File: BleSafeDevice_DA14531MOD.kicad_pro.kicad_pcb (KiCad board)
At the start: 2 copper layers, 43.5 x 33.5 mm, 17 parts, among them J1 SWD_DEBUG_PADS, J2 CURRENT_MEAS_PADS, SW1 PTS526SK15SMTR2 LFS, U4 DA14531MOD-00F01002

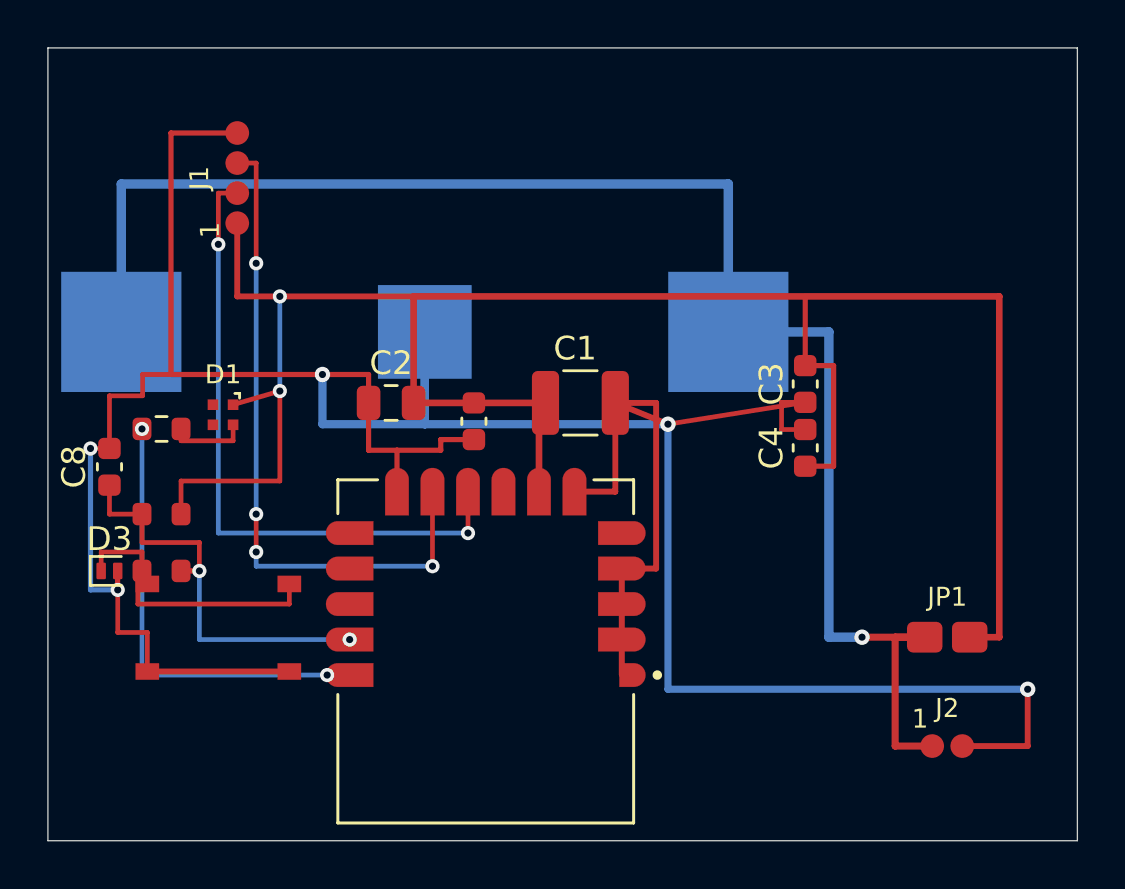
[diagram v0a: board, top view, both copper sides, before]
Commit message: Clear courtyard overlaps for prototype layout
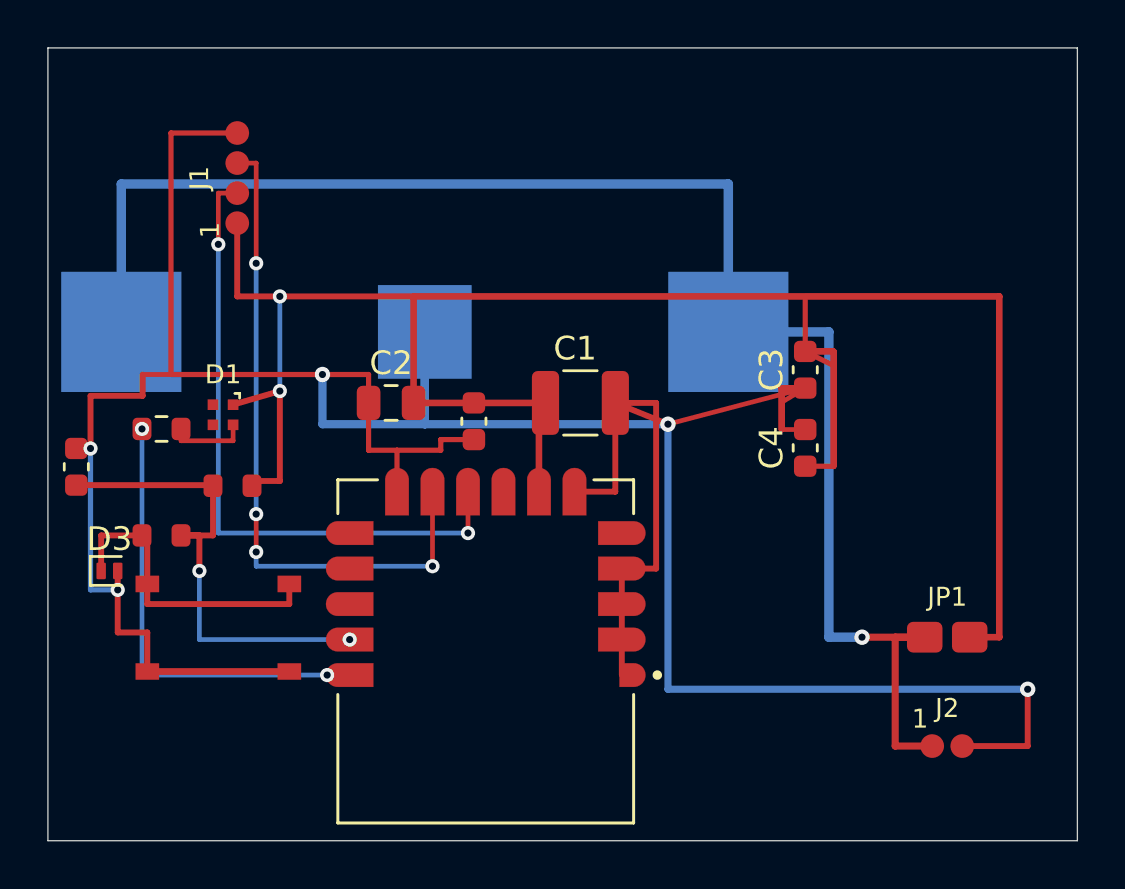
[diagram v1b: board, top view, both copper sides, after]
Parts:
- moved R8 3.23 mm to (106.8, 115.0)
- moved R7 1.50 mm to (103.8, 117.1)
- moved C8 1.40 mm to (100.2, 114.2)
- moved C3 0.60 mm to (131.0, 110.1)
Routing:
- net GND: track 144.8 -> 156.4 mm
- net VCC: track 100.1 -> 107.5 mm
- net /BTN_SW: track 18.2 -> 20.8 mm
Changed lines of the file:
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@@
 	(footprint "Capacitor_SMD:C_0603_1608Metric"
 		(layer "F.Cu")
-		(at 131 110.7 90)
+		(at 131 110.1 90)
 		(descr "Capacitor SMD 0603 (1608 Metric), square (rectangular) end terminal, IPC-7351 nominal, (Body size source: IPC-SM-782 page 76, https://www.pcb-3d.com/wordpress/wp-content/uploads/ipc-sm-782a_amendment_1_and_2.pdf), generated with kicad-footprint-generator")
 		(tags "capacitor")
@@
 	(footprint "Resistor_SMD:R_0603_1608Metric"
 		(layer "F.Cu")
-		(at 103.8 118.6)
+		(at 103.8 117.1)
 		(descr "Resistor SMD 0603 (1608 Metric), square (rectangular) end terminal, IPC-7351 nominal, (Body size source: IPC-SM-782 page 72, https://www.pcb-3d.com/wordpress/wp-content/uploads/ipc-sm-782a_amendment_1_and_2.pdf), generated with kicad-footprint-generator")
 		(tags "resistor")
@@
 	(footprint "Resistor_SMD:R_0603_1608Metric"
 		(layer "F.Cu")
-		(at 103.8 116.2)
+		(at 106.8 115)
 		(descr "Resistor SMD 0603 (1608 Metric), square (rectangular) end terminal, IPC-7351 nominal, (Body size source: IPC-SM-782 page 72, https://www.pcb-3d.com/wordpress/wp-content/uploads/ipc-sm-782a_amendment_1_and_2.pdf), generated with kicad-footprint-generator")
 		(tags "resistor")
@@
 	(footprint "Capacitor_SMD:C_0603_1608Metric"
 		(layer "F.Cu")
-		(at 101.6 114.2 90)
+		(at 100.2 114.2 90)
 		(descr "Capacitor SMD 0603 (1608 Metric), square (rectangular) end terminal, IPC-7351 nominal, (Body size source: IPC-SM-782 page 76, https://www.pcb-3d.com/wordpress/wp-content/uploads/ipc-sm-782a_amendment_1_and_2.pdf), generated with kicad-footprint-generator")
 		(tags "capacitor")
 		(property "Reference" "C8"
-			(at 0 -1.5 90)
+			(at 1.5 0 90)
 			(layer "F.SilkS")
+			(hide yes)
 			(effects
 				(font
@@
 	)
 	(segment
-		(start 101.6 111.2)
-		(end 103 111.2)
-		(width 0.2)
-		(layer "F.Cu")
-		(net 2)
-	)
-	(segment
-		(start 101.95 118.6)
-		(end 101.95 121.2)
-		(width 0.2)
+		(start 103 111.2)
+		(end 103 110.3)
+		(width 0.25)
 		(layer "F.Cu")
 		(net 2)
@@
 	)
 	(segment
+		(start 103.2 121.2)
+		(end 103.2 122.85)
+		(width 0.25)
+		(layer "F.Cu")
+		(net 2)
+	)
+	(segment
+		(start 131 110.875)
+		(end 130 110.875)
+		(width 0.25)
+		(layer "F.Cu")
+		(net 2)
+	)
+	(segment
 		(start 125.2 112.4)
-		(end 131 111.475)
+		(end 131 110.875)
 		(width 0.2)
 		(layer "F.Cu")
@@
 	)
 	(segment
-		(start 131 111.475)
+		(start 101.95 121.2)
+		(end 103.2 121.2)
+		(width 0.25)
+		(layer "F.Cu")
+		(net 2)
+	)
+	(segment
+		(start 131 110.875)
 		(end 130 111.475)
 		(width 0.2)
@@
 	)
 	(segment
+		(start 101.95 119.4)
+		(end 101.95 121.2)
+		(width 0.25)
+		(layer "F.Cu")
+		(net 2)
+	)
+	(segment
 		(start 140.4 126)
 		(end 137.635 126)
@@
 	)
 	(segment
-		(start 101.6 113.425)
-		(end 100.8 113.425)
-		(width 0.2)
+		(start 130 110.875)
+		(end 130 112.625)
+		(width 0.25)
 		(layer "F.Cu")
 		(net 2)
@@
 	)
 	(segment
-		(start 103.2 121.2)
-		(end 103.2 122.85)
-		(width 0.2)
+		(start 100.8 113.425)
+		(end 100.8 111.2)
+		(width 0.25)
+		(layer "F.Cu")
+		(net 2)
+	)
+	(segment
+		(start 131 110.875)
+		(end 130 110.875)
+		(width 0.25)
 		(layer "F.Cu")
 		(net 2)
@@
 	)
 	(segment
-		(start 101.95 121.2)
-		(end 103.2 121.2)
-		(width 0.2)
-		(layer "F.Cu")
-		(net 2)
-	)
-	(segment
 		(start 104.2 100.095)
 		(end 104.2 110.3)
@@
 	)
 	(segment
-		(start 103 111.2)
-		(end 103 110.3)
-		(width 0.2)
+		(start 101.95 118.6)
+		(end 101.95 119.4)
+		(width 0.25)
 		(layer "F.Cu")
 		(net 2)
@@
 	)
 	(segment
+		(start 103.2 122.85)
+		(end 109.2 122.85)
+		(width 0.25)
+		(layer "F.Cu")
+		(net 2)
+	)
+	(segment
 		(start 123.25 121.5)
 		(end 123.25 123)
@@
 	)
 	(segment
-		(start 101.6 113.425)
-		(end 101.6 111.2)
-		(width 0.2)
-		(layer "F.Cu")
-		(net 2)
-	)
-	(segment
 		(start 125.2 112.4)
 		(end 122.975 111.5)
@@
 	)
 	(segment
+		(start 100.2 113.425)
+		(end 100.8 113.425)
+		(width 0.25)
+		(layer "F.Cu")
+		(net 2)
+	)
+	(segment
 		(start 130 112.625)
 		(end 131 112.625)
@@
 	)
 	(segment
-		(start 101.95 119.4)
-		(end 101.95 118.6)
-		(width 0.2)
+		(start 130 110.875)
+		(end 130 112.625)
+		(width 0.25)
 		(layer "F.Cu")
 		(net 2)
@@
 	)
 	(segment
+		(start 100.8 111.2)
+		(end 103 111.2)
+		(width 0.25)
+		(layer "F.Cu")
+		(net 2)
+	)
+	(segment
 		(start 112.55 110.3)
 		(end 112.55 111.5)
@@
 	)
 	(segment
+		(start 107.625 114.8)
+		(end 108.8 114.8)
+		(width 0.25)
+		(layer "F.Cu")
+		(net 3)
+	)
+	(segment
+		(start 108.8 111)
+		(end 106.825 111.575)
+		(width 0.25)
+		(layer "F.Cu")
+		(net 3)
+	)
+	(segment
+		(start 132.199999 109.325)
+		(end 132.199999 114.175)
+		(width 0.25)
+		(layer "F.Cu")
+		(net 3)
+	)
+	(segment
+		(start 131 109.325)
+		(end 132.199999 109.325)
+		(width 0.25)
+		(layer "F.Cu")
+		(net 3)
+	)
+	(segment
+		(start 131 109.325)
+		(end 132.199999 109.325)
+		(width 0.25)
+		(layer "F.Cu")
+		(net 3)
+	)
+	(segment
 		(start 137.95 121.4)
 		(end 139.2 121.4)
@@
 	)
 	(segment
-		(start 104.625 116.2)
-		(end 104.625 114.8)
-		(width 0.2)
-		(layer "F.Cu")
-		(net 3)
-	)
-	(segment
 		(start 139.2 121.4)
 		(end 139.2 107)
@@
 	)
 	(segment
+		(start 108.8 114.8)
+		(end 108.8 111)
+		(width 0.25)
+		(layer "F.Cu")
+		(net 3)
+	)
+	(segment
 		(start 132.199999 109.925)
 		(end 132.199999 114.175)
@@
 	)
 	(segment
-		(start 108.8 111)
-		(end 106.825 111.575)
-		(width 0.2)
+		(start 132.199999 109.325)
+		(end 132.199999 114.175)
+		(width 0.25)
 		(layer "F.Cu")
 		(net 3)
@@
 	)
 	(segment
-		(start 131 109.925)
+		(start 107.625 115)
+		(end 107.625 114.8)
+		(width 0.25)
+		(layer "F.Cu")
+		(net 3)
+	)
+	(segment
+		(start 131 109.325)
 		(end 132.199999 109.925)
 		(width 0.22)
@@
 	)
 	(segment
-		(start 108.8 114.8)
-		(end 108.8 111)
-		(width 0.2)
-		(layer "F.Cu")
-		(net 3)
-	)
-	(segment
 		(start 139.2 107)
 		(end 114.45 107)
@@
 	(segment
 		(start 131 107)
-		(end 131 109.925)
+		(end 131 109.325)
 		(width 0.22)
 		(layer "F.Cu")
@@
 	)
 	(segment
-		(start 104.625 114.8)
-		(end 108.8 114.8)
-		(width 0.2)
-		(layer "F.Cu")
-		(net 3)
-	)
-	(segment
 		(start 139.2 107)
 		(end 131 107)
@@
 	)
 	(segment
-		(start 102.975 116.2)
-		(end 101.6 116.2)
-		(width 0.2)
-		(layer "F.Cu")
-		(net 4)
-	)
-	(segment
-		(start 102.975 117.4)
-		(end 102.975 116.2)
-		(width 0.2)
+		(start 105.4 117.1)
+		(end 105.4 118.6)
+		(width 0.25)
 		(layer "F.Cu")
 		(net 4)
 	)
 	(segment
-		(start 105.4 118.6)
-		(end 105.4 117.4)
-		(width 0.2)
+		(start 100.2 114.975)
+		(end 105.975 114.975)
+		(width 0.25)
 		(layer "F.Cu")
 		(net 4)
 	)
 	(segment
-		(start 104.625 118.6)
-		(end 105.4 118.6)
-		(width 0.2)
+		(start 105.975 114.975)
+		(end 105.975 115)
+		(width 0.25)
 		(layer "F.Cu")
 		(net 4)
 	)
 	(segment
-		(start 104.625 118.6)
-		(end 105.4 118.6)
-		(width 0.2)
+		(start 104.625 117.1)
+		(end 105.4 117.1)
+		(width 0.25)
 		(layer "F.Cu")
 		(net 4)
 	)
 	(segment
-		(start 101.6 116.2)
-		(end 101.6 114.975)
-		(width 0.2)
+		(start 105.975 117.1)
+		(end 104.625 117.1)
+		(width 0.25)
 		(layer "F.Cu")
 		(net 4)
 	)
 	(segment
-		(start 105.4 117.4)
-		(end 102.975 117.4)
-		(width 0.2)
+		(start 105.975 115)
+		(end 105.975 117.1)
+		(width 0.25)
 		(layer "F.Cu")
 		(net 4)
@@
 	)
 	(segment
-		(start 102.8 118.6)
-		(end 102.975 118.6)
-		(width 0.2)
-		(layer "F.Cu")
-		(net 6)
-	)
-	(segment
 		(start 109.2 120)
-		(end 102.8 120)
-		(width 0.2)
+		(end 109.2 119.15)
+		(width 0.25)
 		(layer "F.Cu")
 		(net 6)
 	)
 	(segment
-		(start 102.975 118.6)
-		(end 103.2 119.15)
-		(width 0.2)
+		(start 103.2 119.15)
+		(end 103.2 120)
+		(width 0.25)
 		(layer "F.Cu")
 		(net 6)
 	)
 	(segment
-		(start 102.8 120)
-		(end 102.8 118.6)
-		(width 0.2)
+		(start 101.25 118.6)
+		(end 101.25 117.1)
+		(width 0.25)
 		(layer "F.Cu")
 		(net 6)
 	)
 	(segment
-		(start 109.2 119.15)
-		(end 109.2 120)
-		(width 0.2)
+		(start 101.25 117.1)
+		(end 102.975 117.1)
+		(width 0.25)
 		(layer "F.Cu")
 		(net 6)
 	)
 	(segment
-		(start 101.25 117.8)
-		(end 102.975 117.8)
-		(width 0.2)
+		(start 103.2 120)
+		(end 109.2 120)
+		(width 0.25)
 		(layer "F.Cu")
 		(net 6)
 	)
 	(segment
-		(start 102.975 117.8)
-		(end 102.975 118.6)
-		(width 0.2)
+		(start 103.2 117.1)
+		(end 103.2 119.15)
+		(width 0.25)
 		(layer "F.Cu")
 		(net 6)
 	)
 	(segment
-		(start 101.25 118.6)
-		(end 101.25 117.8)
-		(width 0.2)
+		(start 102.975 117.1)
+		(end 103.2 117.1)
+		(width 0.25)
 		(layer "F.Cu")
 		(net 6)

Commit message: Fix schematic PCB parity for prototype LED simplification
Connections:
- D1 pad 3: (no net) -> unconnected-(D1-GK-Pad3)
- D1 pad 4: (no net) -> unconnected-(D1-BK-Pad4)
- U4 pad J13: (no net) -> unconnected-(U4-P0_7-PadJ13)
- U4 pad J5: (no net) -> unconnected-(U4-P0_6-PadJ5)
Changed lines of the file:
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@@
 	(net 11 "unconnected-(U4-P0_5-PadJ14)")
 	(net 12 "unconnected-(U4-P0_11-PadJ8)")
+	(net 13 "unconnected-(D1-GK-Pad3)")
+	(net 14 "unconnected-(D1-BK-Pad4)")
+	(net 15 "unconnected-(U4-P0_6-PadJ5)")
+	(net 16 "unconnected-(U4-P0_7-PadJ13)")
 	(footprint "SafeGuardPing_Local:TP_1x02_1.27mm_Compact"
 		(layer "F.Cu")
@@
 			(size 0.45 0.45)
 			(layers "F.Cu" "F.Mask" "F.Paste")
+			(net 13 "unconnected-(D1-GK-Pad3)")
 			(solder_mask_margin 0)
 			(solder_paste_margin -0.05)
@@
 			(size 0.45 0.45)
 			(layers "F.Cu" "F.Mask" "F.Paste")
+			(net 14 "unconnected-(D1-BK-Pad4)")
 			(solder_mask_margin 0)
 			(solder_paste_margin -0.05)
@@
 			(size 0.1 0.1)
 			(layers "F.Cu")
+			(net 15 "unconnected-(U4-P0_6-PadJ5)")
 			(pinfunction "P0_6")
 			(pintype "bidirectional")
@@
 			(size 0.1 0.1)
 			(layers "F.Cu")
+			(net 16 "unconnected-(U4-P0_7-PadJ13)")
 			(pinfunction "P0_7")
 			(pintype "bidirectional")

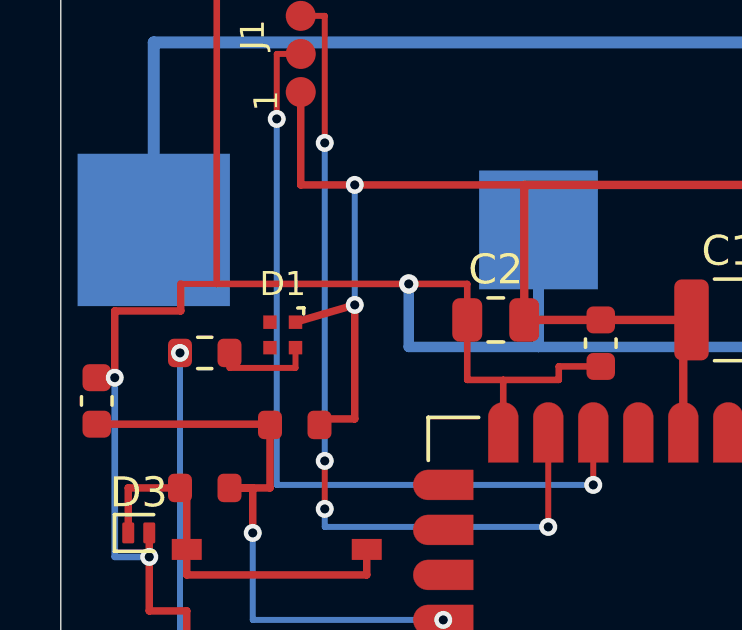
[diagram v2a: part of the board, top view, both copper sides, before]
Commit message: Replace RGB LED with JLC-friendly red 0603 LED
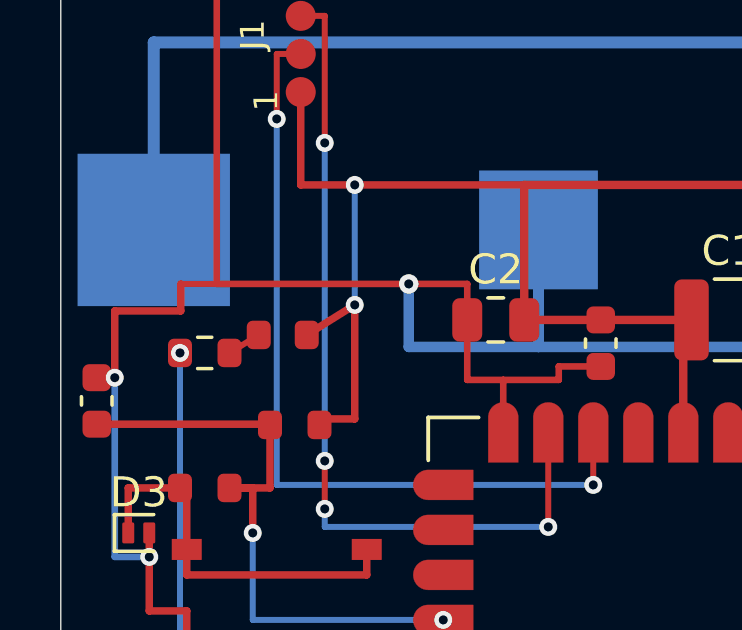
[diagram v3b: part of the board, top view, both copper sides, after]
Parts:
- C3, C4, C5: value 0.1uF 25V -> 100nF 25V
- D1: value LRTBR48G-P9Q7-1 -> Red LED 0603; footprint SafeGuardPing_Local:LED_RGB_amsOSRAM_LRTBR48G -> SafeGuardPing_Local:LED_0603_1608Metric_Red_Generic
- R1: value 1.2K -> 1k
- R8: value 330K -> 330k
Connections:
- D1 pad 1: VCC -> Net-(D1-K)
- D1 pad 2: Net-(D1-RK) -> VCC
- R1 pad 1: Net-(D1-RK) -> Net-(D1-K)
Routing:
- net Net-(D1-RK): track 3.38 -> 0.00 mm
- net Net-(D1-K): track 0.00 -> 1.14 mm

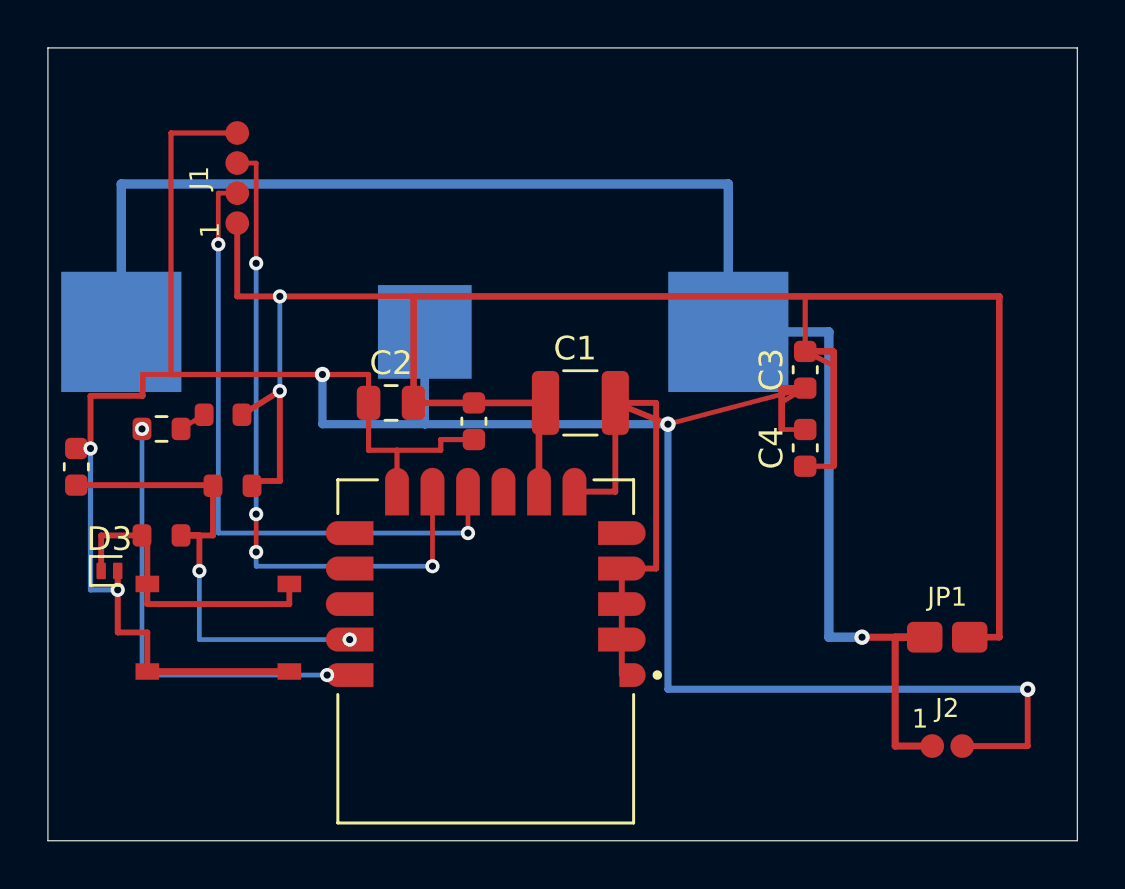
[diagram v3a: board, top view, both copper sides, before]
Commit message: Restore production-close Ping power switch
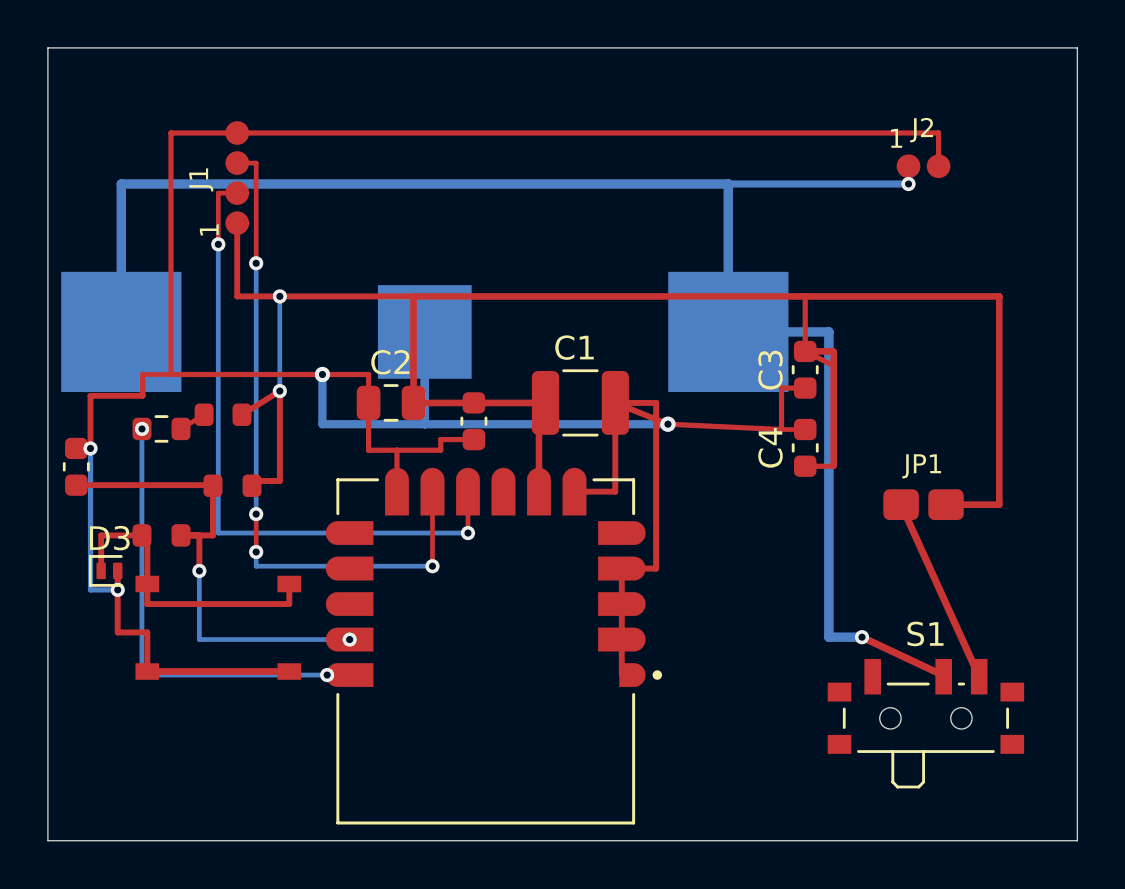
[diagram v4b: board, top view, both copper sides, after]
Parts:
- added S1: SPDT slide power switch PCM12, Button_Switch_SMD:SW_SPDT_PCM12, F.Cu at (136.1, 124.5)
- moved J2 24.5 mm to (136.0, 101.5)
- moved JP1 5.69 mm to (136.0, 115.8)
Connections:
- BT1 pad P1: VBAT -> VBAT_RAW
- BT1 pad P2: VBAT -> VBAT_RAW
- J2 pad 1: VBAT -> VBAT_RAW
- JP1 pad 1: VBAT -> VBAT_SW
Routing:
- net VBAT_RAW: track 0.00 -> 69.0 mm, vias 0 -> 2
- net VBAT: track 66.8 -> 0.00 mm, vias 1 -> 0
- net VCC: track 107.3 -> 94.5 mm
- net VBAT_SW: track 0.00 -> 7.98 mm
- net GND: track 156.4 -> 149.6 mm, vias 5 -> 4
